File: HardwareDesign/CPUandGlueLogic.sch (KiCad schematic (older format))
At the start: 34 parts, among them J100 Conn_01x02, J101 Conn_02x40_Counter_Clockwise, U101 74HCT245, U102 74HCT245, U103 74HCT245, U104 74HCT365, U105 MAX708, U106 HD6809, U107 74HCT00, U108 74HCT27, U109 74HCT138, U110 74HCT138, U111 74HCT138, Y100 Crystal

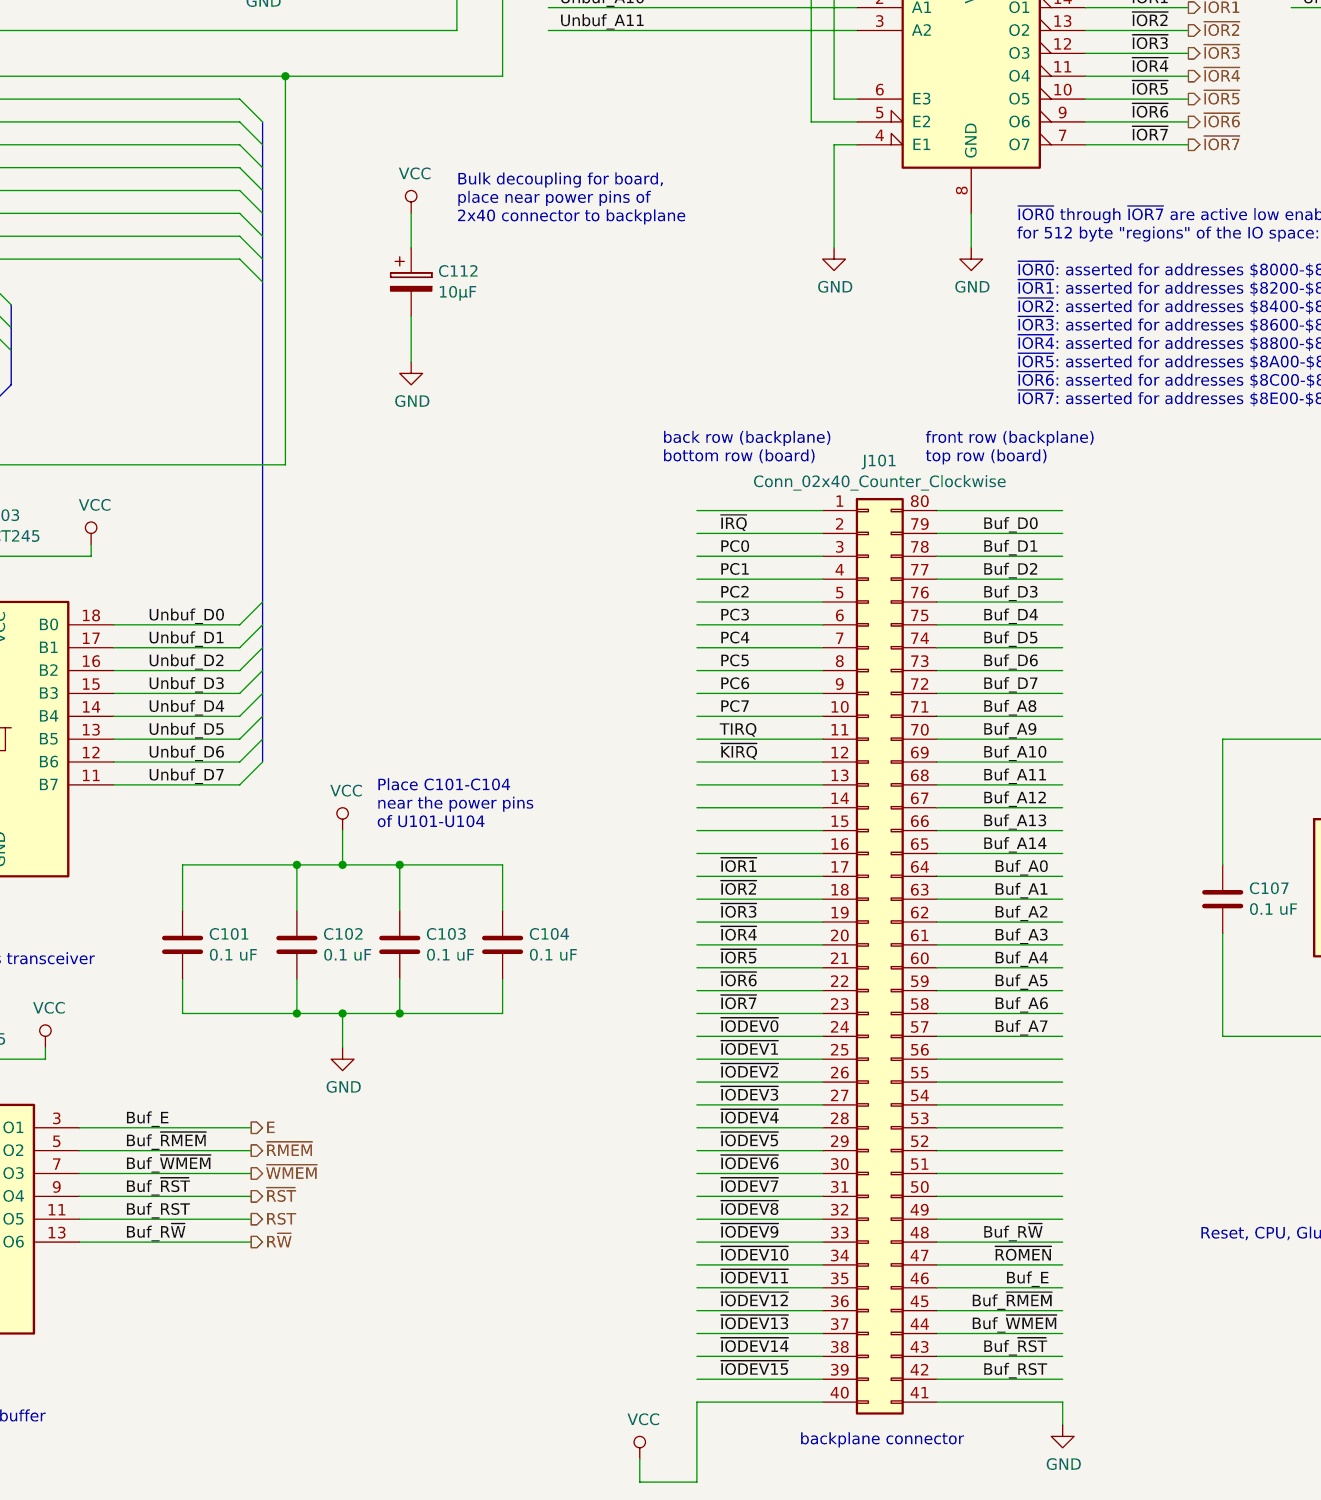
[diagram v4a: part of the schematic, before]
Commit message: have one copy of backplane connector on main sheet
Avoids need to replicate it elsewhere, and helps ensure
that all signals are connected correctly.
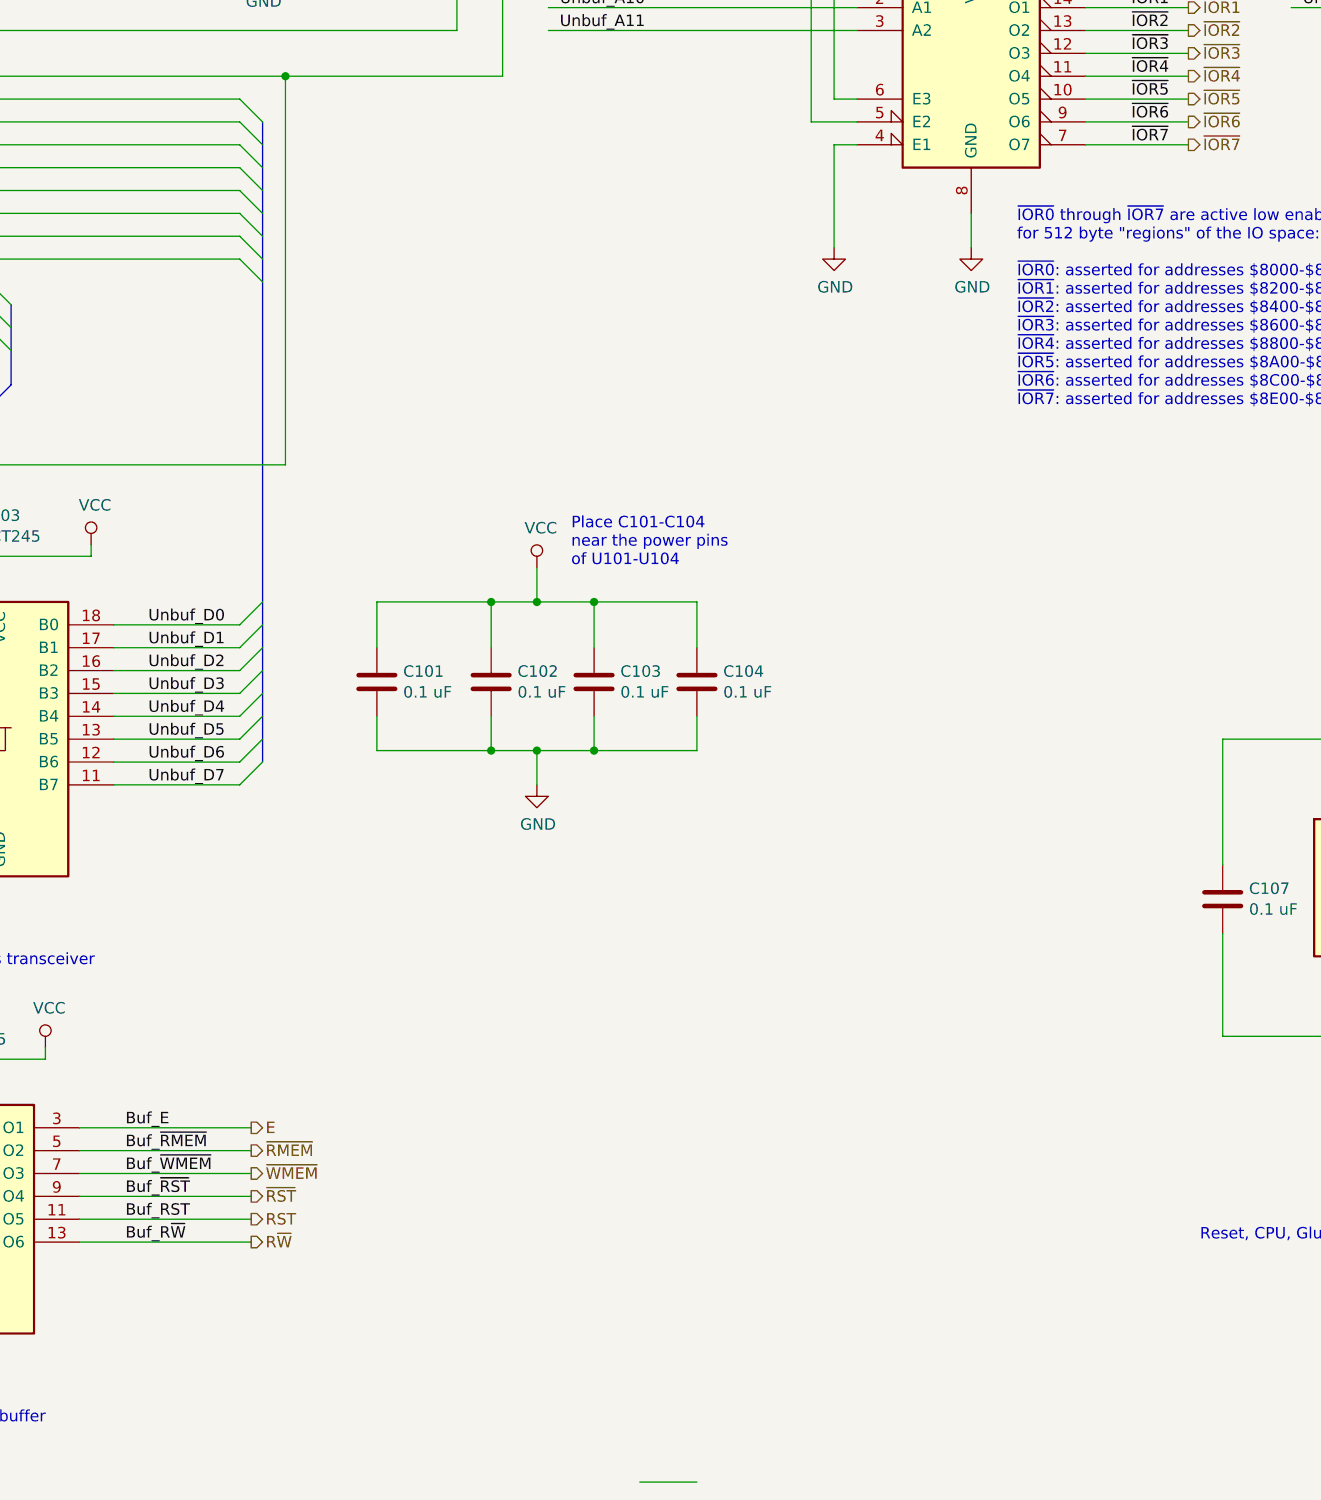
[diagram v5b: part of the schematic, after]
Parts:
- removed C112: 10μF, symbol device:CP
- removed J101: Conn_02x40_Counter_Clockwise, symbol Connector_Generic:Conn_02x40_Counter_Clockwise
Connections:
- net labels removed: PC0, PC1, PC2, PC3, PC4, PC5, PC6, PC7, TIRQ, ~KIRQ~
- wire segments 433 -> 348
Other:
- note removed: "Bulk decoupling for board,\nplace near power pins of\n2x40 connector to backplane"
- note removed: "back row (backplane)\nbottom row (board)"
- note removed: "backplane connector"
- note removed: "front row (backplane)\ntop row (board)"
- moved on the sheet: C101, C102, C103, C104

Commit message: changes to backplane signals
Route all IRQ signals on backplane.

Only route -IOR1..-IOR3 on backplane.

Move TCOUNT2 to after IRQ signals.
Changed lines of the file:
@@
 Wire Wire Line
 	9050 4200 9500 4200
-Wire Wire Line
-	9050 4300 9500 4300
-Wire Wire Line
-	9050 4400 9500 4400
-Wire Wire Line
-	9050 4500 9500 4500
-Wire Wire Line
-	9050 4600 9500 4600
 Text Label 9250 3900 0    50   ~ 0
 ~IOR0~
@@
 Text HLabel 9500 4200 2    50   Output ~ 0
 ~IOR3~
-Text HLabel 9500 4300 2    50   Output ~ 0
-~IOR4~
-Text HLabel 9500 4400 2    50   Output ~ 0
-~IOR5~
-Text HLabel 9500 4500 2    50   Output ~ 0
-~IOR6~
-Text HLabel 9500 4600 2    50   Output ~ 0
-~IOR7~
 $Comp
 L device:C C105
@@
 Wire Wire Line
 	2250 1000 2100 1000
+Wire Wire Line
+	9050 4600 9500 4600
+Wire Wire Line
+	9050 4500 9500 4500
+Wire Wire Line
+	9050 4400 9500 4400
+Wire Wire Line
+	9050 4300 9500 4300
 Wire Bus Line
 	1050 5750 4250 5750

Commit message: assigned component footprints
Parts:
- C101, C102, C103, C104, C105, C106, C107, C108, C109, C110, C111: footprint (none) -> Capacitor_THT:C_Disc_D5.0mm_W2.5mm_P2.50mm
- C113, C114: footprint (none) -> Capacitor_THT:C_Disc_D3.8mm_W2.6mm_P2.50mm
- D100: footprint (none) -> LED_THT:LED_D5.0mm
- J100: footprint (none) -> Connector_PinHeader_2.54mm:PinHeader_1x02_P2.54mm_Vertical
- R100, R101, R102, R103: footprint (none) -> Resistor_THT:R_Axial_DIN0204_L3.6mm_D1.6mm_P7.62mm_Horizontal
- S100: footprint SW_1-1825027-2 -> SW_1-1825027-2:SW_1-1825027-2
- U101, U102, U103: footprint (none) -> Package_DIP:DIP-20_W7.62mm_Socket
- U104, U109, U110, U111: footprint (none) -> Package_DIP:DIP-16_W7.62mm_Socket
- U105: footprint (none) -> Package_DIP:DIP-8_W7.62mm_Socket
- U106: footprint MODULE -> Package_DIP:DIP-40_W15.24mm_Socket
- U107, U108: footprint (none) -> Package_DIP:DIP-14_W7.62mm_Socket
- Y100: footprint (none) -> Crystal:Crystal_HC18-U_Vertical

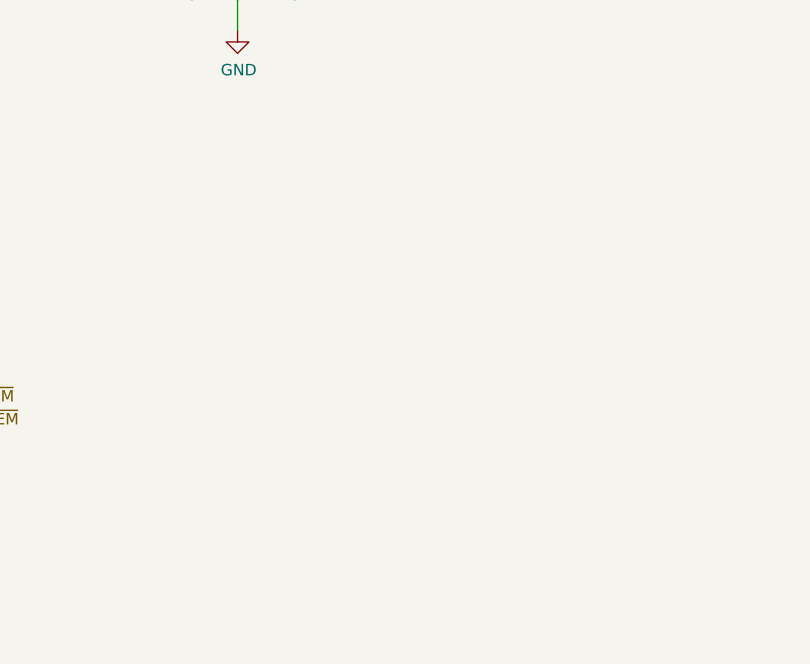
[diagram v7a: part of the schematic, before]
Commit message: add pull-up resistors to data bus signals
This will ensure that they are always at a valid
logic level.
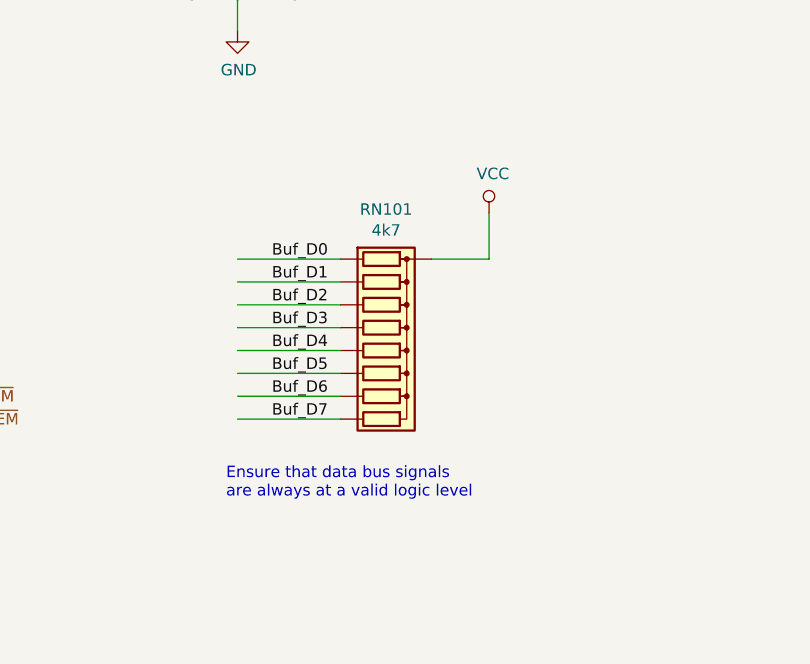
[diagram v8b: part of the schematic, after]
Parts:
- added RN101: 4k7, Resistors_THT:R_Array_SIP9, symbol device:R_Network08
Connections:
- wire segments 348 -> 358
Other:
- note added: "Ensure that data bus signals\nare always at a valid logic level"
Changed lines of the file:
@@
 Wire Wire Line
 	9050 4300 9500 4300
+$Comp
+L device:R_Network08 RN101
+U 1 1 6100A6F1
+P 7300 8800
+F 0 "RN101" V 6683 8800 50  0000 C CNN
+F 1 "4k7" V 6774 8800 50  0000 C CNN
+F 2 "Resistors_THT:R_Array_SIP9" V 7775 8800 50  0001 C CNN
+F 3 "" H 7300 8800 50  0001 C CNN
+	1    7300 8800
+	0    1    1    0
+$EndComp
+Wire Wire Line
+	7100 8400 6650 8400
+Wire Wire Line
+	7100 8500 6650 8500
+Wire Wire Line
+	7100 8600 6650 8600
+Wire Wire Line
+	7100 8700 6650 8700
+Wire Wire Line
+	7100 8800 6650 8800
+Wire Wire Line
+	7100 8900 6650 8900
+Wire Wire Line
+	7100 9000 6650 9000
+Wire Wire Line
+	7100 9100 6650 9100
+Text Label 6800 8400 0    50   ~ 0
+Buf_D0
+Text Label 6800 8500 0    50   ~ 0
+Buf_D1
+Text Label 6800 8600 0    50   ~ 0
+Buf_D2
+Text Label 6800 8700 0    50   ~ 0
+Buf_D3
+Text Label 6800 8800 0    50   ~ 0
+Buf_D4
+Text Label 6800 8900 0    50   ~ 0
+Buf_D5
+Text Label 6800 9000 0    50   ~ 0
+Buf_D6
+Text Label 6800 9100 0    50   ~ 0
+Buf_D7
+Wire Wire Line
+	7500 8400 7750 8400
+Wire Wire Line
+	7750 8400 7750 8200
 Wire Bus Line
 	1050 5750 4250 5750
@@
 Wire Bus Line
 	2700 6200 2700 9250
+$Comp
+L power:VCC #PWR?
+U 1 1 610CD813
+P 7750 8200
+F 0 "#PWR?" H 7750 8050 50  0001 C CNN
+F 1 "VCC" H 7767 8373 50  0000 C CNN
+F 2 "" H 7750 8200 50  0001 C CNN
+F 3 "" H 7750 8200 50  0001 C CNN
+	1    7750 8200
+	1    0    0    -1
+$EndComp
+Text Notes 6600 9450 0    50   ~ 0
+Ensure that data bus signals\nare always at a valid logic level
 $EndSCHEMATC
